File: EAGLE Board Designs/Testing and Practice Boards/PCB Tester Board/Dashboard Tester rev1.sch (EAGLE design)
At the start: 26 parts, among them J1 CONNECTOR-CAN_NF_T_V_BLACK, J2 CONNECTOR-6_NF_T_V_BLACK, J3 CONNECTOR-8_NF_T_V_BLACK, Q1 TRANSISTOR_N_MOS_PMV15ENEA, Q10 TRANSISTOR_N_MOS_PMV15ENEA, Q11 TRANSISTOR_P_MOS_SOT23_SI2369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, Q2 TRANSISTOR_N_MOS_PMV15ENEA, Q3 TRANSISTOR_N_MOS_PMV15ENEA, Q4 TRANSISTOR_N_MOS_PMV15ENEA, Q5 TRANSISTOR_N_MOS_PMV15ENEA, Q6 TRANSISTOR_N_MOS_PMV15ENEA, Q7 TRANSISTOR_P_MOS_SOT23_SI2369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, Q8 TRANSISTOR_N_MOS_PMV15ENEA, Q9 TRANSISTOR_P_MOS_SOT23_SI2369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, U1 TEENSY_3.5, U2 CAN_TRANSCIEVER_TCAN1051HQV-Q1, U3 VOLTAGE_REGULATOR__5V

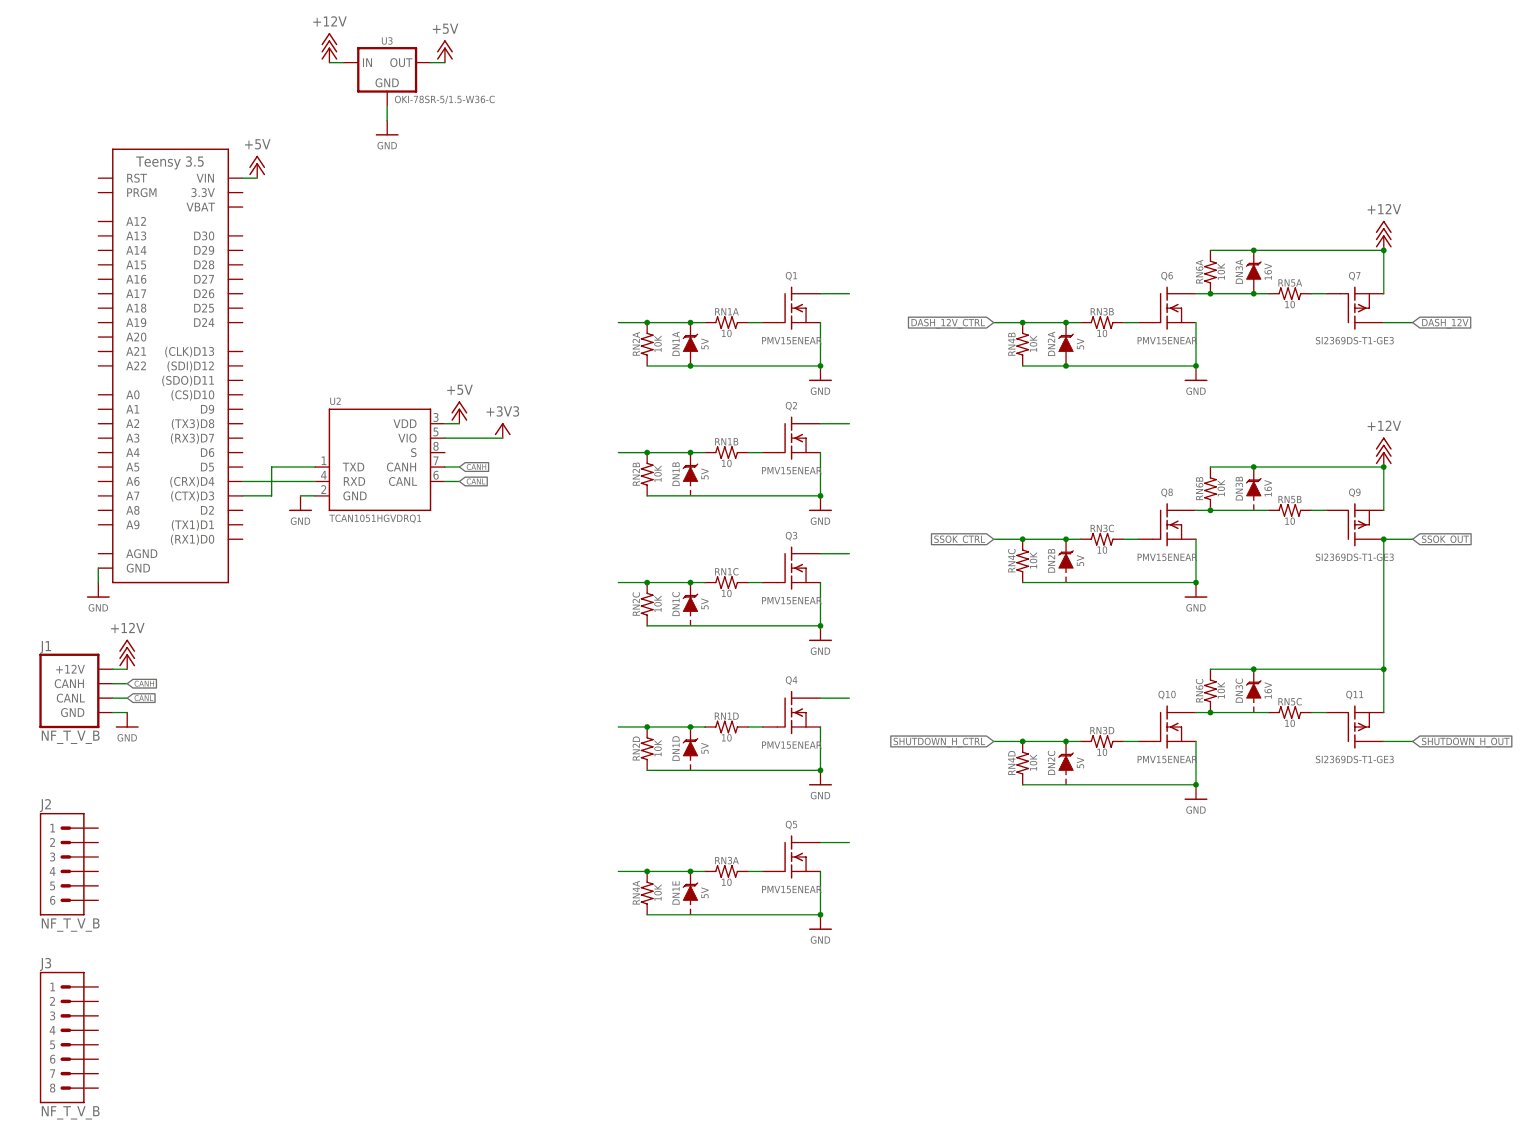
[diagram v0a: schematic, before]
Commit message: Ready to route except for connections to teensy
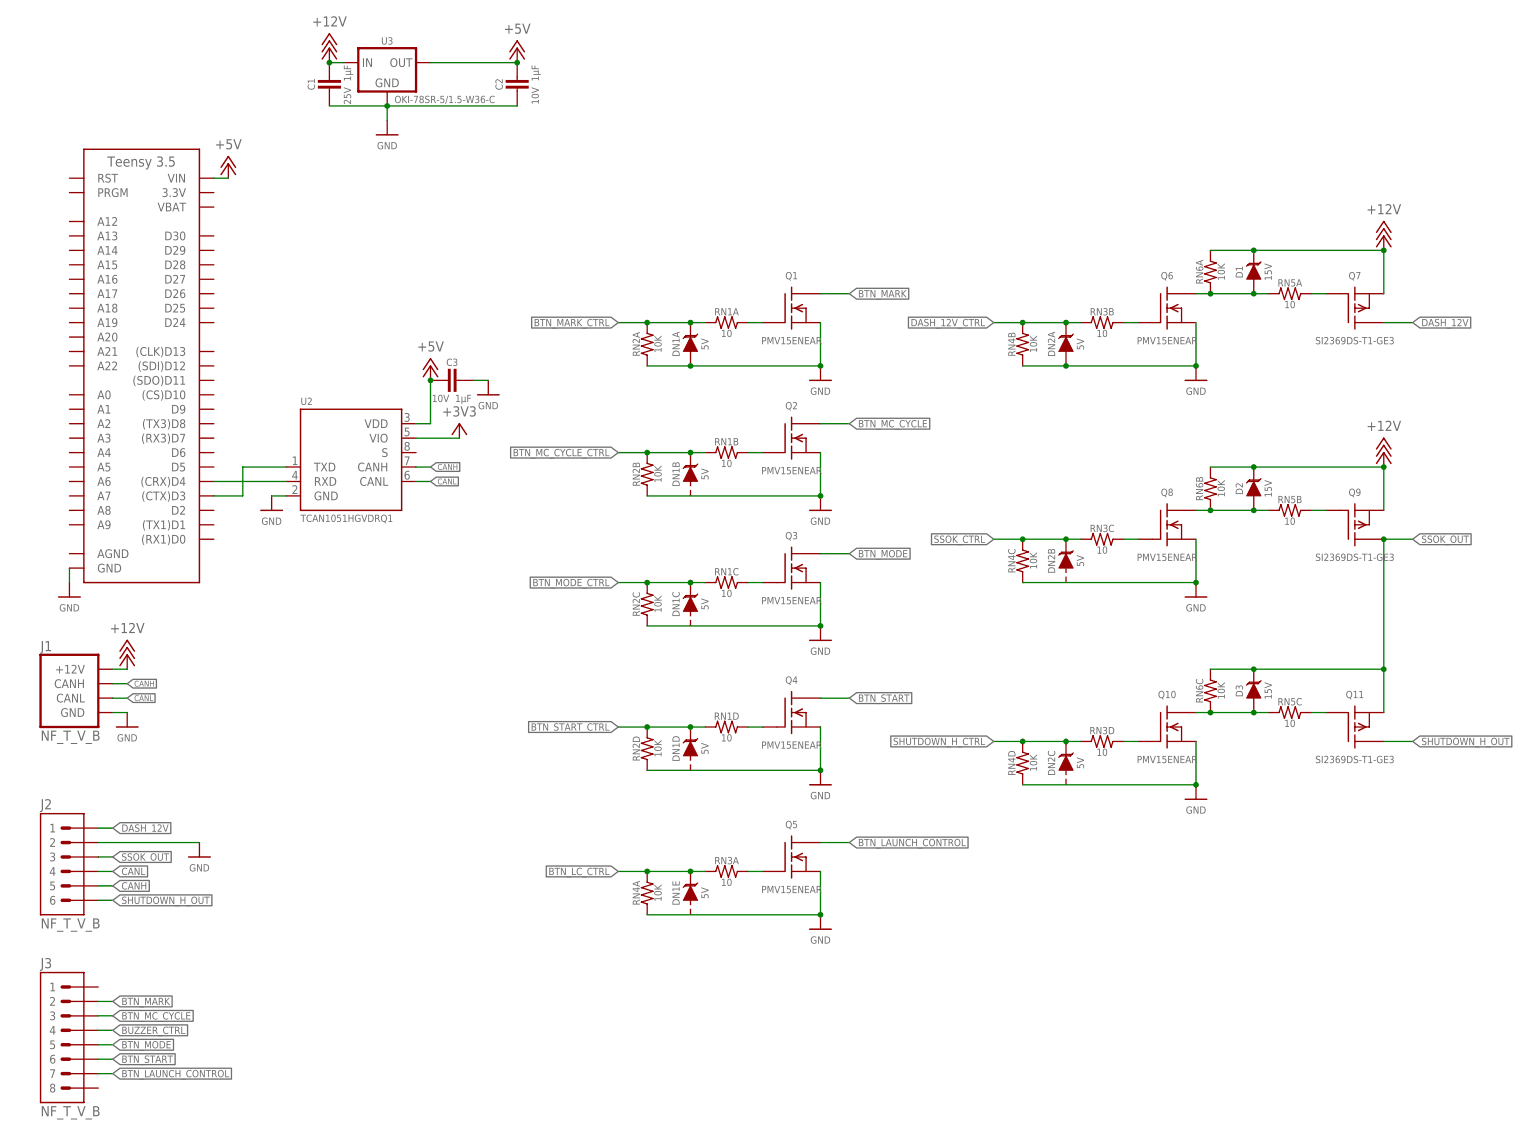
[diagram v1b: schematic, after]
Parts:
- removed DN3: TVS_ARRAY_16V, HyTechDevices:TVS_ARRAY_16V
- added C1: CAPACITOR_0603_25V_1UF, HyTechDevices:CAPACITOR_0603_25V_1UF
- added C2, C3: CAPACITOR_0603_10V_1UF, HyTechDevices:CAPACITOR_0603_10V_1UF
- added D1, D2, D3: TVS_15V, HyTechDevices:TVS_15V
- U3: value VOLTAGE_REGULATOR__5V -> VOLTAGE_REGULATOR_OKI-78SR_5V; device HyTechDevices:VOLTAGE_REGULATOR__5V -> HyTechDevices:VOLTAGE_REGULATOR_OKI-78SR_5V
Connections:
- net N$11 renamed BTN_LC_CTRL
- net N$2 renamed BTN_MARK_CTRL
- net N$5 renamed BTN_MC_CYCLE_CTRL
- net N$7 renamed BTN_MODE_CTRL
- net N$9 renamed BTN_START_CTRL
- removed net N$25: Q5.D
- removed net N$26: Q4.D
- removed net N$27: Q3.D
- removed net N$28: Q2.D
- removed net N$29: Q1.D
- new net BTN_LAUNCH_CONTROL: J3.7, Q5.D
- new net BTN_MARK: J3.2, Q1.D
- new net BTN_MC_CYCLE: J3.3, Q2.D
- new net BTN_MODE: J3.5, Q3.D
- new net BTN_START: J3.6, Q4.D
- new net BUZZER_CTRL: J3.4
- net +12V: now also C1.1, D1.C, D2.C; no longer DN3A.C, DN3B.C
- net +5V: now also C2.1, C3.2
- net CANH: now also J2.5
- net CANL: now also J2.4
- net DASH_12V: now also J2.1
- net GND: now also C1.2, C2.2, C3.1, J2.2
- net N$16: now also D2.A
- net N$19: now also D1.A; no longer DN3A.A
- net N$22: now also D3.A
- net SHUTDOWN_H_OUT: now also J2.6
- net SSOK_OUT: now also D3.C, J2.3; no longer DN3C.C
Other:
- moved on the sheet: U2

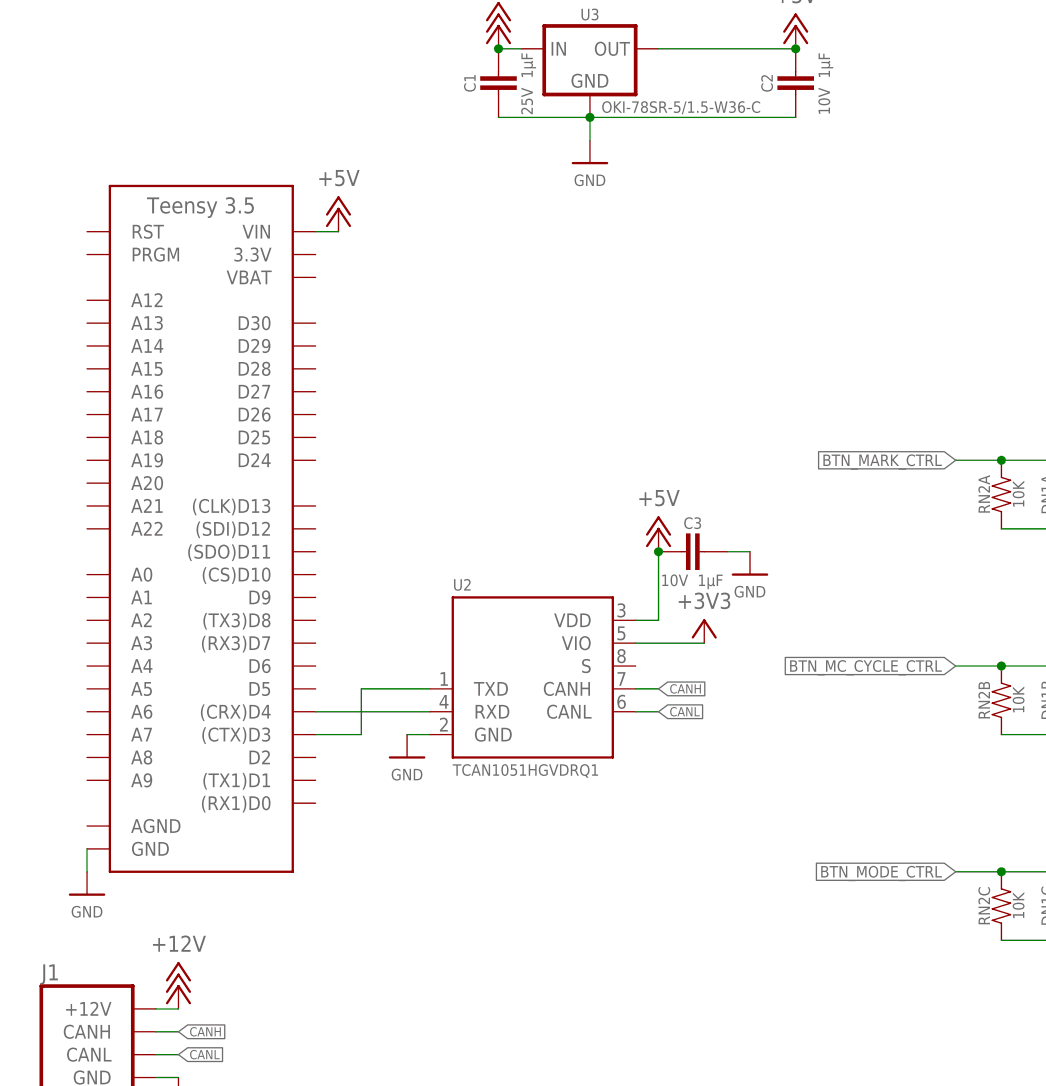
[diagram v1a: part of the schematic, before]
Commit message: Control connections to teensy
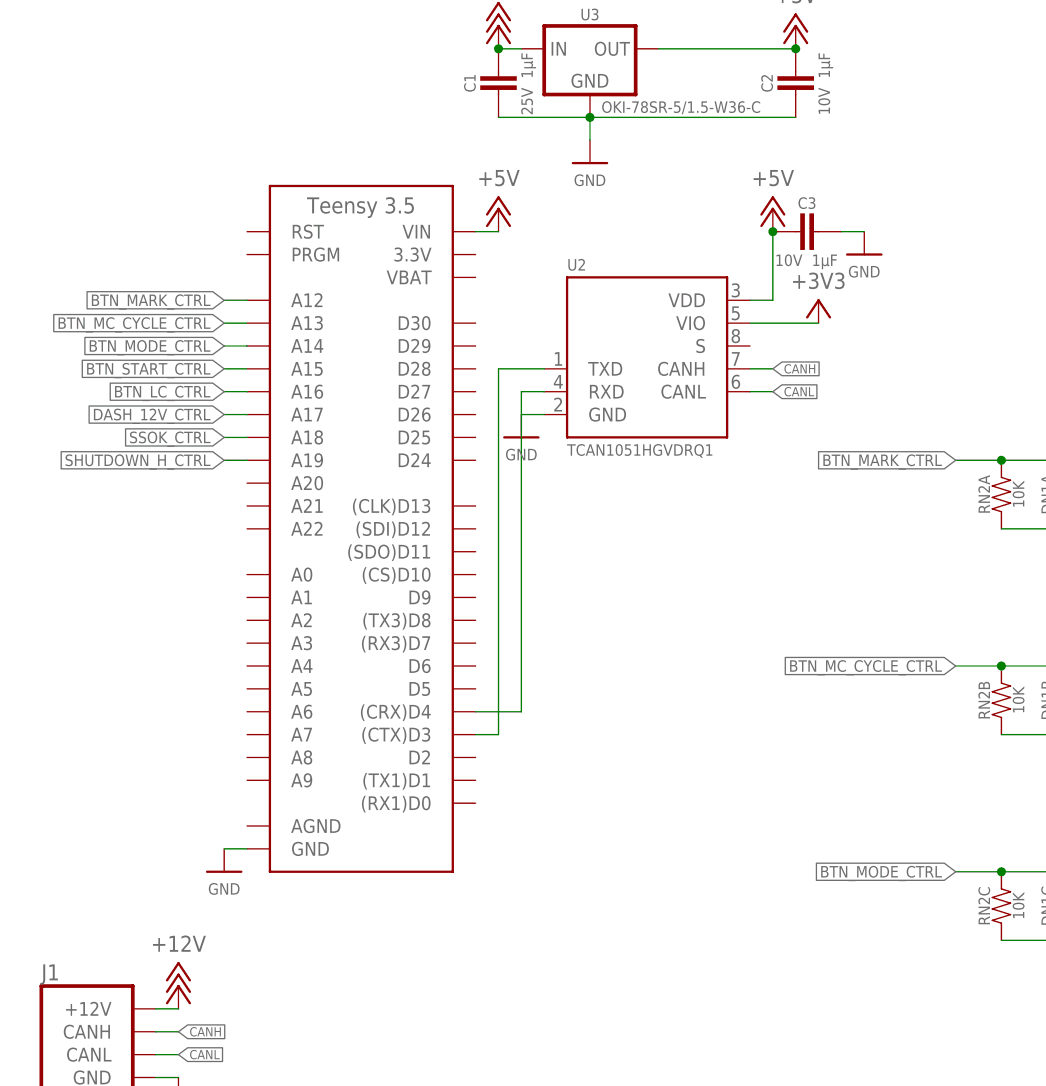
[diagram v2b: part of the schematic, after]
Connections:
- new net N$5: U1.A17
- net BTN_LC_CTRL: now also U1.A16
- net BTN_MARK_CTRL: now also U1.A12
- net BTN_MC_CYCLE_CTRL: now also U1.A13
- net BTN_MODE_CTRL: now also U1.A14
- net BTN_START_CTRL: now also U1.A15
- net SHUTDOWN_H_CTRL: now also U1.A19
- net SSOK_CTRL: now also U1.A18
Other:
- moved on the sheet: C3, U2

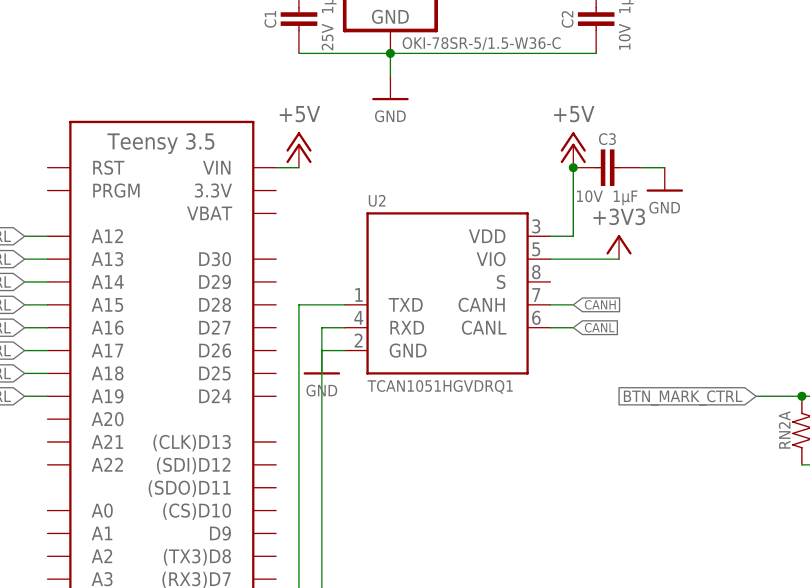
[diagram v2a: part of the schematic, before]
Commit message: Connected buzzer, began tracing
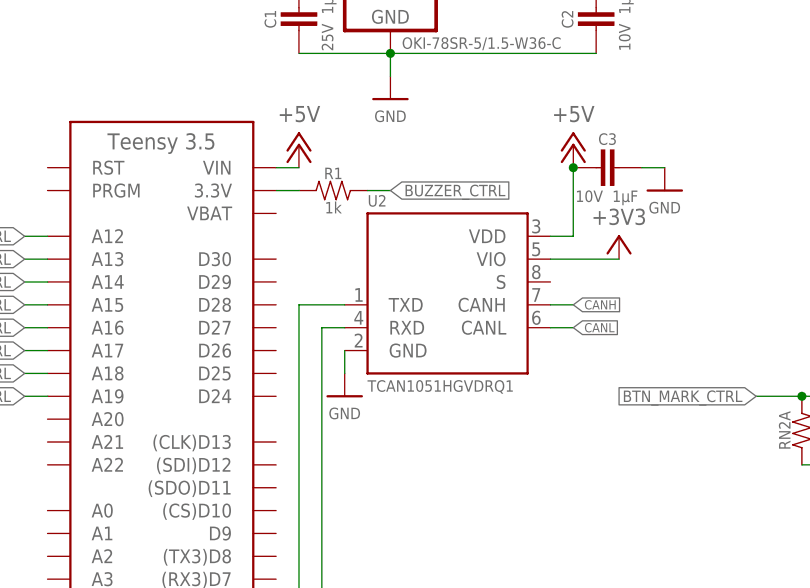
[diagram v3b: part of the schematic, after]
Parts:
- added R1: 1k, HyTechDevices:RESISTOR0603
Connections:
- new net N$7: R1.1, U1.3.3V
- new net N$9: R1.2
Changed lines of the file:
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@@
 <part name="C3" library="HyTechDevices" deviceset="CAPACITOR_?_*" device="0603" technology="10V_1UF"/>
 <part name="GND14" library="HyTechSupplies" deviceset="GND" device=""/>
+<part name="R1" library="HyTechDevices" deviceset="RESISTOR" device="0603" value="1k"/>
 </parts>
 <sheets>
@@
 <attribute name="VALUE" x="27.94" y="77.47" size="1.27" layer="96" align="top-center"/>
 </instance>
-<instance part="GND11" gate="1" x="66.04" y="152.4" smashed="yes">
-<attribute name="VALUE" x="66.04" y="151.13" size="1.27" layer="96" align="top-center"/>
+<instance part="GND11" gate="1" x="68.58" y="149.86" smashed="yes">
+<attribute name="VALUE" x="68.58" y="148.59" size="1.27" layer="96" align="top-center"/>
 </instance>
 <instance part="GND12" gate="1" x="73.66" y="182.88" smashed="yes">
@@
 <instance part="GND14" gate="1" x="104.14" y="172.72" smashed="yes">
 <attribute name="VALUE" x="104.14" y="171.45" size="1.27" layer="96" align="top-center"/>
+</instance>
+<instance part="R1" gate="G$1" x="68.58" y="172.72" smashed="yes">
+<attribute name="NAME" x="67.31" y="173.99" size="1.27" layer="95" align="bottom-center"/>
+<attribute name="VALUE" x="67.31" y="171.45" size="1.27" layer="96" align="top-center"/>
 </instance>
 </instances>
@@
 <pinref part="U2" gate="G$1" pin="GND"/>
 <pinref part="GND11" gate="1" pin="GND"/>
-<wire x1="68.58" y1="154.94" x2="66.04" y2="154.94" width="0.1524" layer="91"/>
+<wire x1="68.58" y1="154.94" x2="68.58" y2="152.4" width="0.1524" layer="91"/>
 </segment>
 <segment>
@@
 <wire x1="22.86" y1="25.4" x2="25.4" y2="25.4" width="0.1524" layer="91"/>
 <label x="25.4" y="25.4" size="1.27" layer="95" xref="yes"/>
+<label x="73.66" y="172.72" size="1.27" layer="95" xref="yes"/>
 </segment>
 </net>
@@
 </segment>
 </net>
+<net name="N$7" class="0">
+<segment>
+<pinref part="U1" gate="G$1" pin="3.3V"/>
+<pinref part="R1" gate="G$1" pin="1"/>
+<wire x1="60.96" y1="172.72" x2="63.5" y2="172.72" width="0.1524" layer="91"/>
+</segment>
+</net>
+<net name="N$9" class="0">
+<segment>
+<pinref part="R1" gate="G$1" pin="2"/>
+<wire x1="71.12" y1="172.72" x2="73.66" y2="172.72" width="0.1524" layer="91"/>
+</segment>
+</net>
